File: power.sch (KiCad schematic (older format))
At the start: 21 parts, among them P1 CONN_01X02, P2 CONN_01X02, P23 CONN_01X02, P24 CONN_01X02, P3 CONN_01X02, P4 CONN_01X02, U1 ST1S14PHR

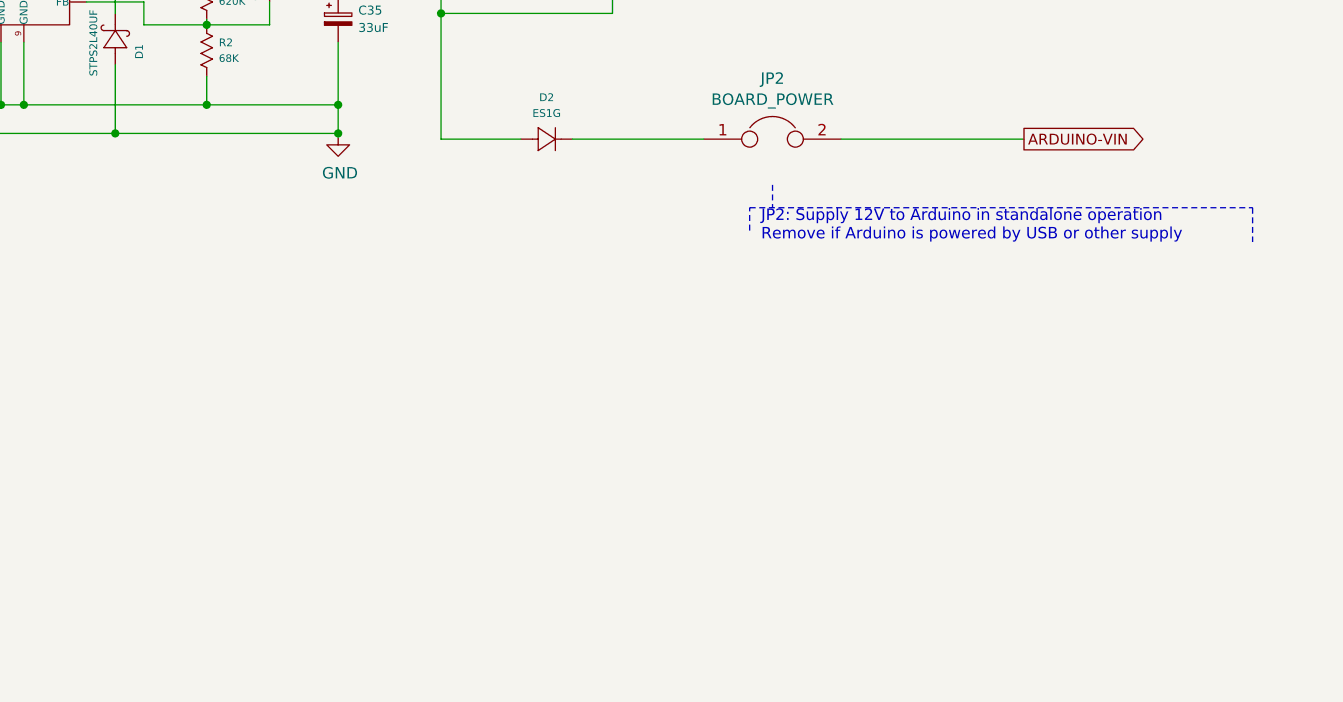
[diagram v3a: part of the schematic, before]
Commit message: Added minimal arduino mega support
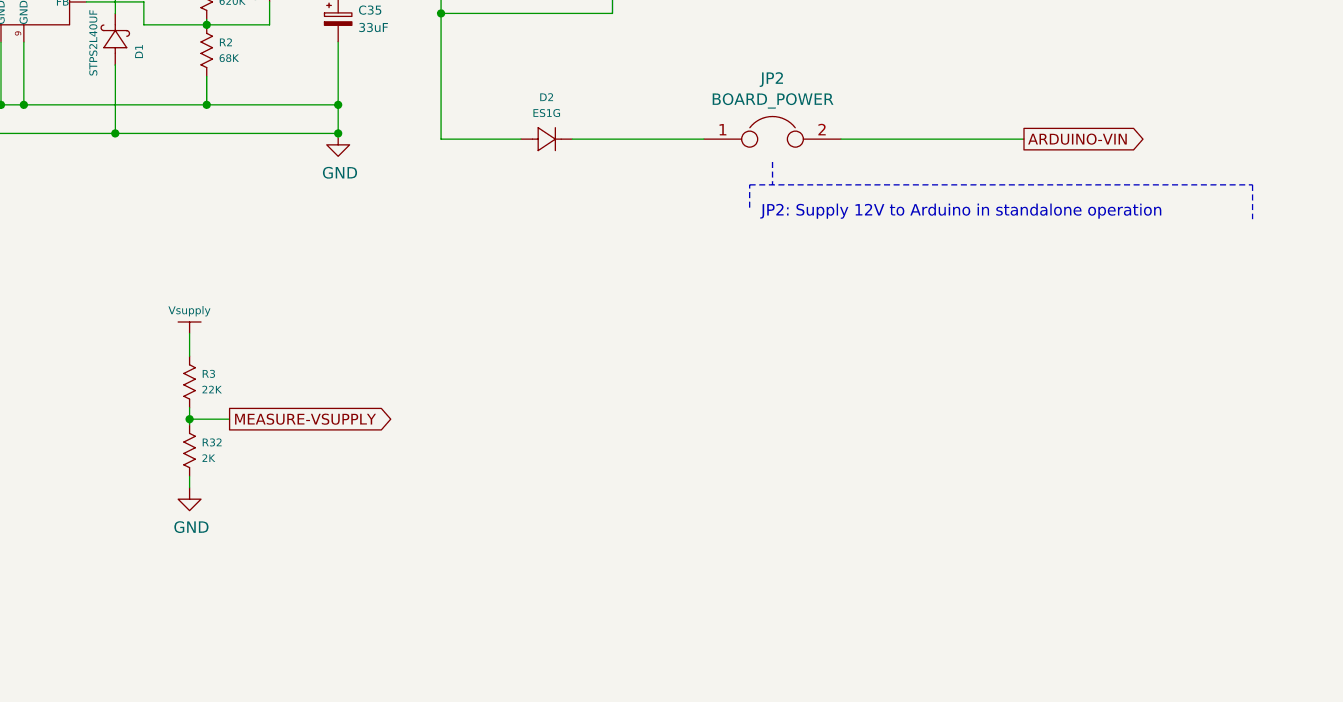
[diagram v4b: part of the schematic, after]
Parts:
- added R3: 22K, resistors:R_0603, symbol RESISTOR
- added R32: 2K, resistors:R_0603, symbol RESISTOR
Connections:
- net GND: now also R32.2
- net Vsupply: now also R3.1
- new net MEASURE-VSUPPLY: R3.2, R32.1
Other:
- note added: "JP2: Supply 12V to Arduino in standalone operation\n"
- note removed: "JP2: Supply 12V to Arduino in standalone operation\nRemove if Arduino is powered by USB or other supply"
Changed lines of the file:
@@
 Text GLabel 6950 2625 2    47   Output ~ 0
 ARDUINO-VIN
-Text Notes 5800 3075 0    50   ~ 0
-JP2: Supply 12V to Arduino in standalone operation\nRemove if Arduino is powered by USB or other supply
-Wire Notes Line
-	5850 2825 5850 2925
-Wire Notes Line
-	5750 3025 5750 2925
-Wire Notes Line
-	5750 2925 7950 2925
-Wire Notes Line
-	7950 2925 7950 3075
+Wire Notes Line
+	5850 2725 5850 2825
+Wire Notes Line
+	5750 2925 5750 2825
+Wire Notes Line
+	5750 2825 7950 2825
+Wire Notes Line
+	7950 2825 7950 2975
 Wire Notes Line
 	4600 1625 5000 1625
@@
 $EndComp
 $Comp
-L +12V #PWR15
+L +12V #PWR16
 U 1 1 568AC408
 P 5150 1925
-F 0 "#PWR15" H 5150 1775 50  0001 C CNN
+F 0 "#PWR16" H 5150 1775 50  0001 C CNN
 F 1 "+12V" H 5168 2099 50  0000 C CNN
 F 2 "" H 5150 1925 50  0000 C CNN
@@
 	1500 4350 1425 4350
 $Comp
-L Vsupply #P6
+L Vsupply #P7
 U 1 1 568AD53F
 P 4750 1225
-F 0 "#P6" H 4750 1225 60  0001 C CNN
+F 0 "#P7" H 4750 1225 60  0001 C CNN
 F 1 "Vsupply" H 4750 1175 34  0000 C CNN
 F 2 "" H 4750 1225 60  0000 C CNN
@@
 Connection ~ 2375 2475
 $Comp
-L GND #PWR14
+L GND #PWR15
 U 1 1 56BE0E01
 P 3950 2600
-F 0 "#PWR14" H 3950 2350 50  0001 C CNN
+F 0 "#PWR15" H 3950 2350 50  0001 C CNN
 F 1 "GND" H 3958 2426 50  0000 C CNN
 F 2 "" H 3950 2600 50  0000 C CNN
@@
 Wire Wire Line
 	3300 1825 4150 1825
+Text Notes 5800 2975 0    50   ~ 0
+JP2: Supply 12V to Arduino in standalone operation\n
+$Comp
+L Vsupply #P6
+U 1 1 56C4E641
+P 3300 3325
+F 0 "#P6" H 3300 3325 60  0001 C CNN
+F 1 "Vsupply" H 3300 3275 34  0000 C CNN
+F 2 "" H 3300 3325 60  0000 C CNN
+F 3 "" H 3300 3325 60  0000 C CNN
+	1    3300 3325
+	1    0    0    -1
+$EndComp
+$Comp
+L RESISTOR R3
+U 1 1 56C4E772
+P 3225 3575
+F 0 "R3" V 3303 3703 34  0000 L CNN
+F 1 "22K" V 3372 3703 33  0000 L CNN
+F 2 "resistors:R_0603" H 3225 3575 60  0001 C CNN
+F 3 "" H 3225 3575 60  0000 C CNN
+	1    3225 3575
+	0    1    1    0
+$EndComp
+$Comp
+L RESISTOR R32
+U 1 1 56C4E7F8
+P 3225 3875
+F 0 "R32" V 3303 4003 34  0000 L CNN
+F 1 "2K" V 3372 4003 33  0000 L CNN
+F 2 "resistors:R_0603" H 3225 3875 60  0001 C CNN
+F 3 "" H 3225 3875 60  0000 C CNN
+	1    3225 3875
+	0    1    1    0
+$EndComp
+$Comp
+L GND #PWR14
+U 1 1 56C4EA68
+P 3300 4150
+F 0 "#PWR14" H 3300 3900 50  0001 C CNN
+F 1 "GND" H 3308 3976 50  0000 C CNN
+F 2 "" H 3300 4150 50  0000 C CNN
+F 3 "" H 3300 4150 50  0000 C CNN
+	1    3300 4150
+	1    0    0    -1
+$EndComp
+Wire Wire Line
+	3300 4150 3300 4100
+Wire Wire Line
+	3300 3875 3300 3800
+Wire Wire Line
+	3300 3575 3300 3475
+Text GLabel 3475 3850 2    47   Output ~ 0
+MEASURE-VSUPPLY
+Wire Wire Line
+	3475 3850 3300 3850
+Connection ~ 3300 3850
 $EndSCHEMATC

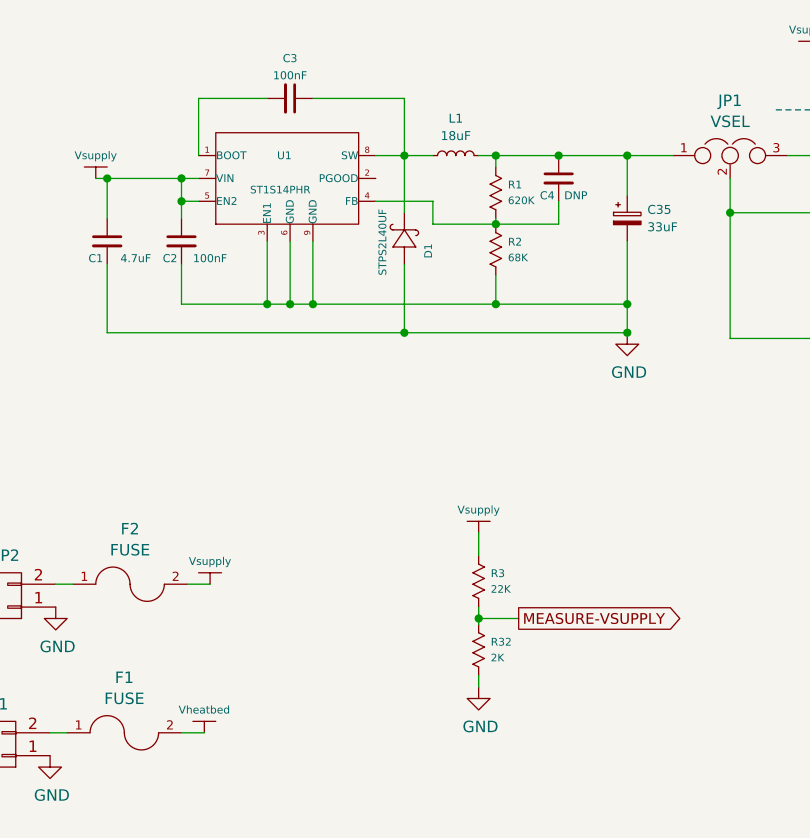
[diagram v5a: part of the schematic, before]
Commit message: Added component specifications
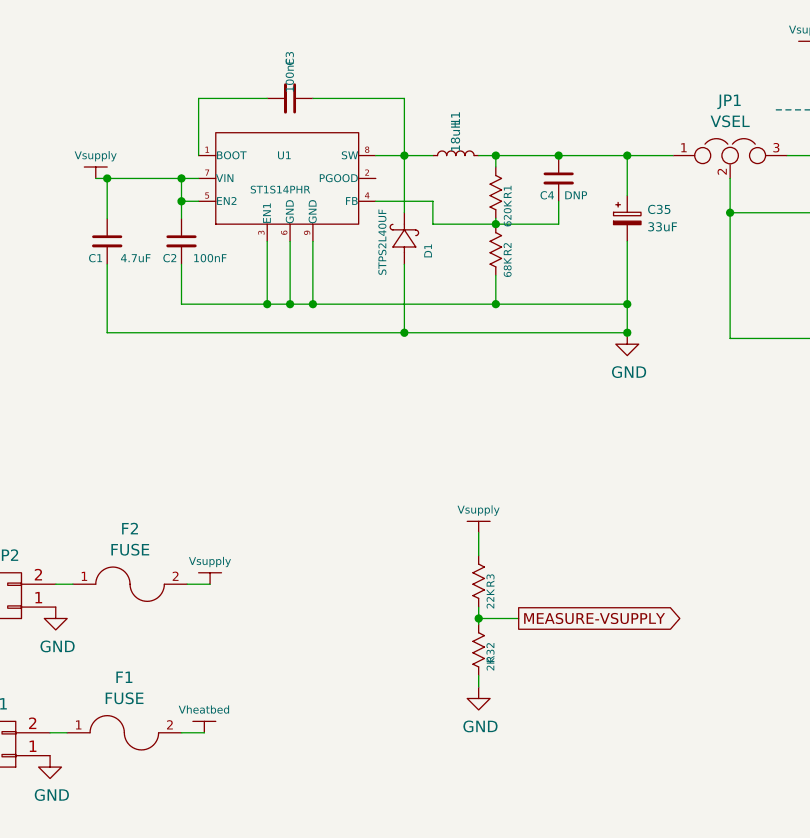
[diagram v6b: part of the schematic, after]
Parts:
- C2, C3: Specification (none) -> X7R; VoltageRating (none) -> 50V
- C35: Manufacturer (none) -> Panasonic; ManufacturerNo (none) -> EEE-FK1E330W
- D1: Manufacturer (none) -> ST Microelectronics; ManufacturerNo (none) -> STPS2L40UF
- D2: Manufacturer (none) -> Fairchild Semiconductor; ManufacturerNo (none) -> ES1G
- F1, F2: Manufacturer (none) -> Keystone; ManufacturerNo (none) -> 3557
- L1: value 18uF -> 18uH; Manufacturer (none) -> Bourns; ManufacturerNo (none) -> RLB0914-180KL
- R1, R2, R3, R32: Specification (none) -> 1%
- U1: Manufacturer (none) -> ST Microelectronics; ManufacturerNo (none) -> ST1S14PHR
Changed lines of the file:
@@
 F 2 "diodes:DO214AA_SMB" H 3025 2300 60  0001 C CNN
 F 3 "" H 3025 2300 60  0000 C CNN
+F 4 "ST Microelectronics" H 3025 2300 135 0001 L CNN "Manufacturer"
+F 5 "STPS2L40UF" H 3025 2300 135 0001 L CNN "ManufacturerNo"
 	1    3025 2300
 	0    -1   -1   0
@@
 F 2 "diodes:DO214AC_SMA" H 4750 2675 60  0001 C CNN
 F 3 "" H 4750 2675 60  0000 C CNN
+F 4 "Fairchild Semiconductor" H 4750 2675 135 0001 L CNN "Manufacturer"
+F 5 "ES1G" H 4750 2675 135 0001 L CNN "ManufacturerNo"
 	1    4750 2675
 	1    0    0    -1
@@
 F 2 "misc:FUSEHOLDER_MINI_KEYSTONE_3557" H 1750 4350 50  0001 C CNN
 F 3 "" H 1750 4350 50  0000 C CNN
+F 4 "Keystone" H 1750 4350 135 0001 L CNN "Manufacturer"
+F 5 "3557" H 1750 4350 135 0001 L CNN "ManufacturerNo"
 	1    1750 4350
 	1    0    0    -1
@@
 F 2 "misc:FUSEHOLDER_MINI_KEYSTONE_3557" H 1775 3700 50  0001 C CNN
 F 3 "" H 1775 3700 50  0000 C CNN
+F 4 "Keystone" H 1775 3700 135 0001 L CNN "Manufacturer"
+F 5 "3557" H 1775 3700 135 0001 L CNN "ManufacturerNo"
 	1    1775 3700
 	1    0    0    -1
@@
 U 1 1 56BDE087
 P 2075 2200
-AR Path="/56BDE087" Ref="U1"  Part="1"
-AR Path="/568AA436/56BDE087" Ref="U1"  Part="1"
 F 0 "U1" H 2450 2575 34  0000 C CNN
 F 1 "ST1S14PHR" H 2300 2425 33  0000 L CNN
@@
 F 5 "Armin van der Togt" H 2775 2850 34  0001 L BNN "author"
 F 6 "48V 850kHz 3A switching regulator" H 2775 2750 34  0001 L BNN "description"
+F 7 "ST Microelectronics" H 2075 2200 135 0001 L CNN "Manufacturer"
+F 8 "ST1S14PHR" H 2075 2200 135 0001 L CNN "ManufacturerNo"
 	1    2075 2200
 	1    0    0    -1
@@
 U 1 1 56BDE999
 P 2475 1575
-F 0 "C3" V 2300 1575 35  0000 C CNN
-F 1 "100nF" V 2375 1575 35  0000 C CNN
+F 0 "C3" H 2300 1575 35  0000 C CNN
+F 1 "100nF" H 2375 1575 35  0000 C CNN
 F 2 "capacitors:C_0603" H 2475 1575 50  0001 C CNN
 F 3 "" H 2475 1575 50  0000 C CNN
+F 4 "50V" H 2475 1575 135 0001 L CNN "VoltageRating"
+F 5 "X7R" H 2475 1575 135 0001 L CNN "Specification"
 	1    2475 1575
 	0    1    1    0
@@
 F 2 "capacitors:C_0603" H 2000 2200 50  0001 C CNN
 F 3 "" H 2000 2200 50  0000 C CNN
+F 4 "50V" H 2000 2200 135 0001 L CNN "VoltageRating"
+F 5 "X7R" H 2000 2200 135 0001 L CNN "Specification"
 	1    2000 2200
 	1    0    0    -1
@@
 U 1 1 56BDF21B
 P 3300 1875
-F 0 "R1" V 3378 2003 34  0000 L CNN
-F 1 "620K" V 3447 2003 33  0000 L CNN
+F 0 "R1" H 3378 2003 34  0000 L CNN
+F 1 "620K" H 3447 2003 33  0000 L CNN
 F 2 "resistors:R_0603" H 3300 1875 60  0001 C CNN
 F 3 "" H 3300 1875 60  0000 C CNN
+F 4 "1%" H 3300 1875 135 0001 L CNN "Specification"
 	1    3300 1875
 	0    1    1    0
@@
 U 1 1 56BDF391
 P 3300 2125
-F 0 "R2" V 3378 2253 34  0000 L CNN
-F 1 "68K" V 3447 2253 33  0000 L CNN
+F 0 "R2" H 3378 2253 34  0000 L CNN
+F 1 "68K" H 3447 2253 33  0000 L CNN
 F 2 "resistors:R_0603" H 3300 2125 60  0001 C CNN
 F 3 "" H 3300 2125 60  0000 C CNN
+F 4 "1%" H 3300 2125 135 0001 L CNN "Specification"
 	1    3300 2125
 	0    1    1    0
@@
 F 2 "capacitors:c_elec_6.3x7.7" H 3950 2100 50  0001 C CNN
 F 3 "" H 3950 2100 50  0000 C CNN
+F 4 "Panasonic" H 3950 2100 135 0001 L CNN "Manufacturer"
+F 5 "EEE-FK1E330W" H 3950 2100 135 0001 L CNN "ManufacturerNo"
 	1    3950 2100
 	1    0    0    -1
@@
 U 1 1 56BDF1D2
 P 3200 1825
-F 0 "L1" V 3362 1825 39  0000 C CNN
-F 1 "18uF" V 3286 1825 39  0000 C CNN
-F 2 "inductors:INDUCTOR_BOURNS_RLB914" V 3294 1825 50  0001 C CNN
+F 0 "L1" H 3362 1825 39  0000 C CNN
+F 1 "18uH" H 3286 1825 39  0000 C CNN
+F 2 "inductors:INDUCTOR_BOURNS_RLB914" H 3294 1825 50  0001 C CNN
 F 3 "" H 3200 1825 50  0000 C CNN
+F 4 "Bourns" H 3200 1825 135 0001 L CNN "Manufacturer"
+F 5 "RLB0914-180KL" H 3200 1825 135 0001 L CNN "ManufacturerNo"
 	1    3200 1825
 	0    -1   -1   0
@@
 U 1 1 56C4E772
 P 3225 3575
-F 0 "R3" V 3303 3703 34  0000 L CNN
-F 1 "22K" V 3372 3703 33  0000 L CNN
+F 0 "R3" H 3303 3703 34  0000 L CNN
+F 1 "22K" H 3372 3703 33  0000 L CNN
 F 2 "resistors:R_0603" H 3225 3575 60  0001 C CNN
 F 3 "" H 3225 3575 60  0000 C CNN
+F 4 "1%" H 3225 3575 135 0001 L CNN "Specification"
 	1    3225 3575
 	0    1    1    0
@@
 U 1 1 56C4E7F8
 P 3225 3875
-F 0 "R32" V 3303 4003 34  0000 L CNN
-F 1 "2K" V 3372 4003 33  0000 L CNN
+F 0 "R32" H 3303 4003 34  0000 L CNN
+F 1 "2K" H 3372 4003 33  0000 L CNN
 F 2 "resistors:R_0603" H 3225 3875 60  0001 C CNN
 F 3 "" H 3225 3875 60  0000 C CNN
+F 4 "1%" H 3225 3875 135 0001 L CNN "Specification"
 	1    3225 3875
 	0    1    1    0

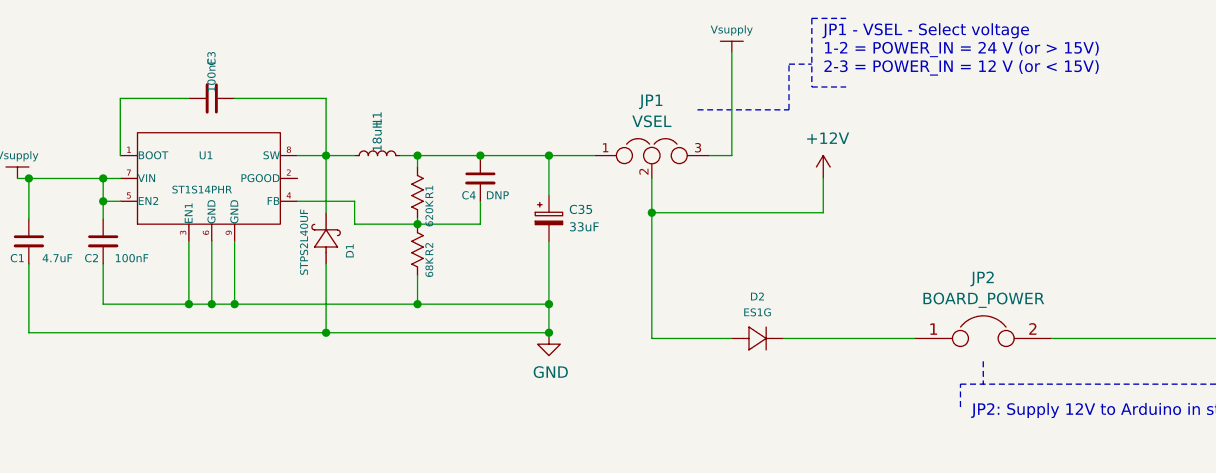
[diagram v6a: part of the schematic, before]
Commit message: Added specifications and manufacturers to component attributes
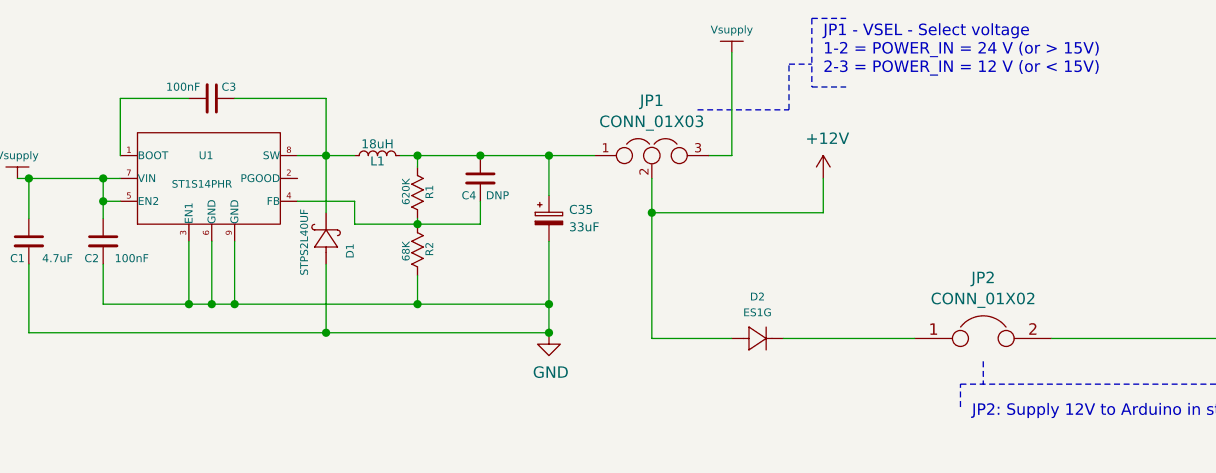
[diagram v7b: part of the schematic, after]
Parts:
- C1: Manufacturer (none) -> Murata; ManufacturerNo (none) -> GRM32ER71H475KA88L
- C4: Comment (none) -> Do not place; Specification (none) -> Do Not Place
- F1, F2: Specification (none) -> 2pcs Keystone 3557
- JP1: value VSEL -> CONN_01X03; Comment (none) -> VSEL; Specification (none) -> 3 pin 2.54mm pitch single row male header
- JP2: value BOARD_POWER -> CONN_01X02; Comment (none) -> BOARD_POWER; Specification (none) -> 2 pin 2.54mm pitch single row male header
- P1, P2: Manufacturer (none) -> Phoenix contact; ManufacturerNo (none) -> 1923869
- P23, P24, P3, P4: Specification (none) -> 2 pin 2.54mm pitch single row male header
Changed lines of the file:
@@
 P 4400 1825
 F 0 "JP1" H 4400 2065 50  0000 C CNN
-F 1 "VSEL" H 4400 1973 50  0000 C CNN
+F 1 "CONN_01X03" H 4400 1973 50  0000 C CNN
 F 2 "headers:CON_HDR_1x3_2.54mm" H 4400 1825 50  0001 C CNN
 F 3 "" H 4400 1825 50  0000 C CNN
+F 4 "VSEL" H 4400 1825 135 0001 L CNN "Comment"
+F 5 "3 pin 2.54mm pitch single row male header" H 4400 1825 135 0001 L CNN "Specification"
 	1    4400 1825
 	1    0    0    -1
@@
 P 5850 2625
 F 0 "JP2" H 5850 2890 50  0000 C CNN
-F 1 "BOARD_POWER" H 5850 2798 50  0000 C CNN
+F 1 "CONN_01X02" H 5850 2798 50  0000 C CNN
 F 2 "headers:CON_HDR_1x2_2.54mm" H 5850 2625 50  0001 C CNN
 F 3 "" H 5850 2625 50  0000 C CNN
+F 4 "BOARD_POWER" H 5850 2625 135 0001 L CNN "Comment"
+F 5 "2 pin 2.54mm pitch single row male header" H 5850 2625 135 0001 L CNN "Specification"
 	1    5850 2625
 	1    0    0    -1
@@
 F 2 "terminal_blocks:CON_PHOENIX_MSTBA-2.5-2-G-5.08" H 1225 4400 50  0001 C CNN
 F 3 "" H 1225 4400 50  0000 C CNN
+F 4 "Phoenix contact" H 1225 4400 135 0001 L CNN "Manufacturer"
+F 5 "1923869" H 1225 4400 135 0001 L CNN "ManufacturerNo"
 	1    1225 4400
 	-1   0    0    1
@@
 F 4 "Keystone" H 1750 4350 135 0001 L CNN "Manufacturer"
 F 5 "3557" H 1750 4350 135 0001 L CNN "ManufacturerNo"
+F 6 "2pcs Keystone 3557" H 1750 4350 135 0001 L CNN "Specification"
 	1    1750 4350
 	1    0    0    -1
@@
 F 2 "terminal_blocks:CON_PHOENIX_MSTBA-2.5-2-G-5.08" H 1250 3750 50  0001 C CNN
 F 3 "" H 1250 3750 50  0000 C CNN
+F 4 "Phoenix contact" H 1250 3750 135 0001 L CNN "Manufacturer"
+F 5 "1923869" H 1250 3750 135 0001 L CNN "ManufacturerNo"
 	1    1250 3750
 	-1   0    0    1
@@
 F 4 "Keystone" H 1775 3700 135 0001 L CNN "Manufacturer"
 F 5 "3557" H 1775 3700 135 0001 L CNN "ManufacturerNo"
+F 6 "2pcs Keystone 3557" H 1775 3700 135 0001 L CNN "Specification"
 	1    1775 3700
 	1    0    0    -1
@@
 F 2 "headers:CON_HDR_1x2_2.54mm" H 1350 5225 50  0001 C CNN
 F 3 "" H 1350 5225 50  0000 C CNN
+F 4 "2 pin 2.54mm pitch single row male header" H 1350 5225 135 0001 L CNN "Specification"
 	1    1350 5225
 	-1   0    0    1
@@
 F 2 "headers:CON_HDR_1x2_2.54mm" H 1350 6375 50  0001 C CNN
 F 3 "" H 1350 6375 50  0000 C CNN
+F 4 "2 pin 2.54mm pitch single row male header" H 1350 6375 135 0001 L CNN "Specification"
 	1    1350 6375
 	-1   0    0    1
@@
 F 2 "headers:CON_HDR_1x2_2.54mm" H 1350 5750 50  0001 C CNN
 F 3 "" H 1350 5750 50  0000 C CNN
+F 4 "2 pin 2.54mm pitch single row male header" H 1350 5750 135 0001 L CNN "Specification"
 	1    1350 5750
 	-1   0    0    1
@@
 F 2 "headers:CON_HDR_1x2_2.54mm" H 1350 7000 50  0001 C CNN
 F 3 "" H 1350 7000 50  0000 C CNN
+F 4 "2 pin 2.54mm pitch single row male header" H 1350 7000 135 0001 L CNN "Specification"
 	1    1350 7000
 	-1   0    0    1
@@
 P 2075 2200
 F 0 "U1" H 2450 2575 34  0000 C CNN
-F 1 "ST1S14PHR" H 2300 2425 33  0000 L CNN
+F 1 "ST1S14PHR" H 2300 2450 33  0000 L CNN
 F 2 "soic:HSOP8" H 2075 2200 60  0001 C CNN
 F 3 "" H 2075 2200 60  0000 C CNN
@@
 U 1 1 56BDE999
 P 2475 1575
-F 0 "C3" H 2300 1575 35  0000 C CNN
-F 1 "100nF" H 2375 1575 35  0000 C CNN
+F 0 "C3" V 2425 1650 35  0000 C CNN
+F 1 "100nF" V 2425 1450 35  0000 C CNN
 F 2 "capacitors:C_0603" H 2475 1575 50  0001 C CNN
 F 3 "" H 2475 1575 50  0000 C CNN
@@
 P 3300 1875
 F 0 "R1" H 3378 2003 34  0000 L CNN
-F 1 "620K" H 3447 2003 33  0000 L CNN
+F 1 "620K" H 3350 1900 33  0000 L CNN
 F 2 "resistors:R_0603" H 3300 1875 60  0001 C CNN
 F 3 "" H 3300 1875 60  0000 C CNN
@@
 P 3300 2125
 F 0 "R2" H 3378 2253 34  0000 L CNN
-F 1 "68K" H 3447 2253 33  0000 L CNN
+F 1 "68K" H 3375 2150 33  0000 L CNN
 F 2 "resistors:R_0603" H 3300 2125 60  0001 C CNN
 F 3 "" H 3300 2125 60  0000 C CNN
@@
 F 2 "capacitors:C_1210" H 1675 2200 50  0001 C CNN
 F 3 "" H 1675 2200 50  0000 C CNN
+F 4 "Murata" H 1675 2200 135 0001 L CNN "Manufacturer"
+F 5 "GRM32ER71H475KA88L" H 1675 2200 135 0001 L CNN "ManufacturerNo"
 	1    1675 2200
 	1    0    0    -1
@@
 F 2 "capacitors:C_0603" H 3650 1925 50  0001 C CNN
 F 3 "" H 3650 1925 50  0000 C CNN
+F 4 "Do Not Place" H 3650 1925 135 0001 L CNN "Specification"
+F 5 "Do not place" H 3650 1925 135 0001 L CNN "Comment"
 	1    3650 1925
 	1    0    0    -1
@@
 U 1 1 56BDF1D2
 P 3200 1825
-F 0 "L1" H 3362 1825 39  0000 C CNN
-F 1 "18uH" H 3286 1825 39  0000 C CNN
+F 0 "L1" V 3175 1825 39  0000 C CNN
+F 1 "18uH" V 3250 1825 39  0000 C CNN
 F 2 "inductors:INDUCTOR_BOURNS_RLB914" H 3294 1825 50  0001 C CNN
 F 3 "" H 3200 1825 50  0000 C CNN
